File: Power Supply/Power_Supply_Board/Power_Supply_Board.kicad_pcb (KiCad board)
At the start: 2 copper layers, 36 parts

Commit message: Power Supply Board Progress
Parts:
- C1, C3: footprint Capacitor_THT:CP_Axial_L30.0mm_D18.0mm_P35.00mm_Horizontal -> Capacitor_THT:CP_Axial_L55.0mm_D26.0mm_P60.00mm_Horizontal
- C2, C4: footprint Capacitor_THT:CP_Axial_L30.0mm_D18.0mm_P35.00mm_Horizontal -> Capacitor_THT:CP_Axial_L55.0mm_D26.0mm_P60.00mm_Horizontal; moved to B.Cu
- C5, C6, C7: footprint Capacitor_THT:CP_Axial_L38.0mm_D21.0mm_P44.00mm_Horizontal -> Capacitor_THT:CP_Axial_L42.0mm_D26.0mm_P45.00mm_Horizontal
- moved C3 59.4 mm to (150.3, 115.3), turned to 180 degrees
- moved TP12 56.9 mm to (180.8, 85.7)
- moved R1 49.0 mm to (97.4, 101.0)
- moved C4 47.7 mm to (150.3, 119.0), turned to 180 degrees
- moved R2 44.7 mm to (122.8, 101.0)
- moved D2 42.1 mm to (81.4, 121.8)
- moved D1 41.6 mm to (81.4, 135.5)
- moved D6 41.3 mm to (89.1, 145.7), turned to 90 degrees
- moved D4 39.9 mm to (85.3, 121.8)
- moved D5 39.5 mm to (92.9, 145.7), turned to 90 degrees
- moved D3 39.3 mm to (85.3, 135.5)
- moved TP1 36.1 mm to (83.3, 97.7)
- moved TP10 34.6 mm to (81.3, 149.9)
- moved TP11 31.5 mm to (85.5, 149.9)
- moved C7 30.5 mm to (222.4, 137.6)
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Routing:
- net Net-(C1-Pad2): track 0.00 -> 81.2 mm
- net Net-(D2-K): track 0.00 -> 70.8 mm
- net F: track 0.00 -> 31.5 mm
- net G: track 0.00 -> 28.8 mm
- net B: track 0.00 -> 28.1 mm
- net C: track 0.00 -> 27.9 mm
- net Net-(C8-Pad2): track 0.00 -> 24.2 mm
- net D: track 0.00 -> 20.3 mm
- net Net-(D6-A): track 0.00 -> 8.88 mm
- net 60VAC: track 0.00 -> 8.14 mm
- net Net-(D5-A): track 0.00 -> 4.97 mm
- net Net-(D3-A): track 0.00 -> 4.39 mm
- net Net-(D1-A): track 0.00 -> 4.37 mm
- net Net-(D1-K): track 0.00 -> 3.53 mm
- net Net-(D3-K): track 0.00 -> 3.53 mm
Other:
- board text added: "HCF Power Supply"
- board text added: "Might not need the reservoir cap labels. just keep a little buffer on the edge, but otherwise, order doesnt matter just polarity"
- board text added: "Ver 1.0"

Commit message: Power Supply Board Progress
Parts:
- moved C1 3.95 mm to (90.3, 86.7)
- moved C2 3.95 mm to (90.3, 82.7)
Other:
- board text removed: "Might not need the reservoir cap labels. just keep a little buffer on the edge, but otherwise, order doesnt matter just polarity"
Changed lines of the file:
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@@
 	(footprint "Capacitor_THT:CP_Axial_L55.0mm_D26.0mm_P60.00mm_Horizontal"
 		(layer "F.Cu")
-		(at 90.302 82.7075)
+		(at 90.3 86.6525)
 		(descr "CP, Axial series, Axial, Horizontal, pin pitch=60mm, , length*diameter=55*26mm^2, Electrolytic Capacitor, , http://www.vishay.com/docs/42037/53d.pdf")
 		(tags "CP Axial series Axial Horizontal pin pitch 60mm  length 55mm diameter 26mm Electrolytic Capacitor")
@@
 	(footprint "Capacitor_THT:CP_Axial_L55.0mm_D26.0mm_P60.00mm_Horizontal"
 		(layer "B.Cu")
-		(at 90.3 86.6525)
+		(at 90.302 82.7075)
 		(descr "CP, Axial series, Axial, Horizontal, pin pitch=60mm, , length*diameter=55*26mm^2, Electrolytic Capacitor, , http://www.vishay.com/docs/42037/53d.pdf")
 		(tags "CP Axial series Axial Horizontal pin pitch 60mm  length 55mm diameter 26mm Electrolytic Capacitor")
@@
 		)
 		(property "Value" "220uF 300V"
-			(at 30.43 -2.4 180)
+			(at 30.348 1.7475 180)
 			(layer "B.SilkS")
 			(effects
@@
 			)
 			(justify left bottom)
-		)
-	)
-	(gr_text "Might not need the reservoir cap labels. just keep a little buffer on the edge, but otherwise, order doesnt matter just polarity"
-		(at 94.2 72.26 0)
-		(layer "Edge.Cuts")
-		(effects
-			(font
-				(size 1 1)
-				(thickness 0.15)
-			)
-			(justify left bottom)

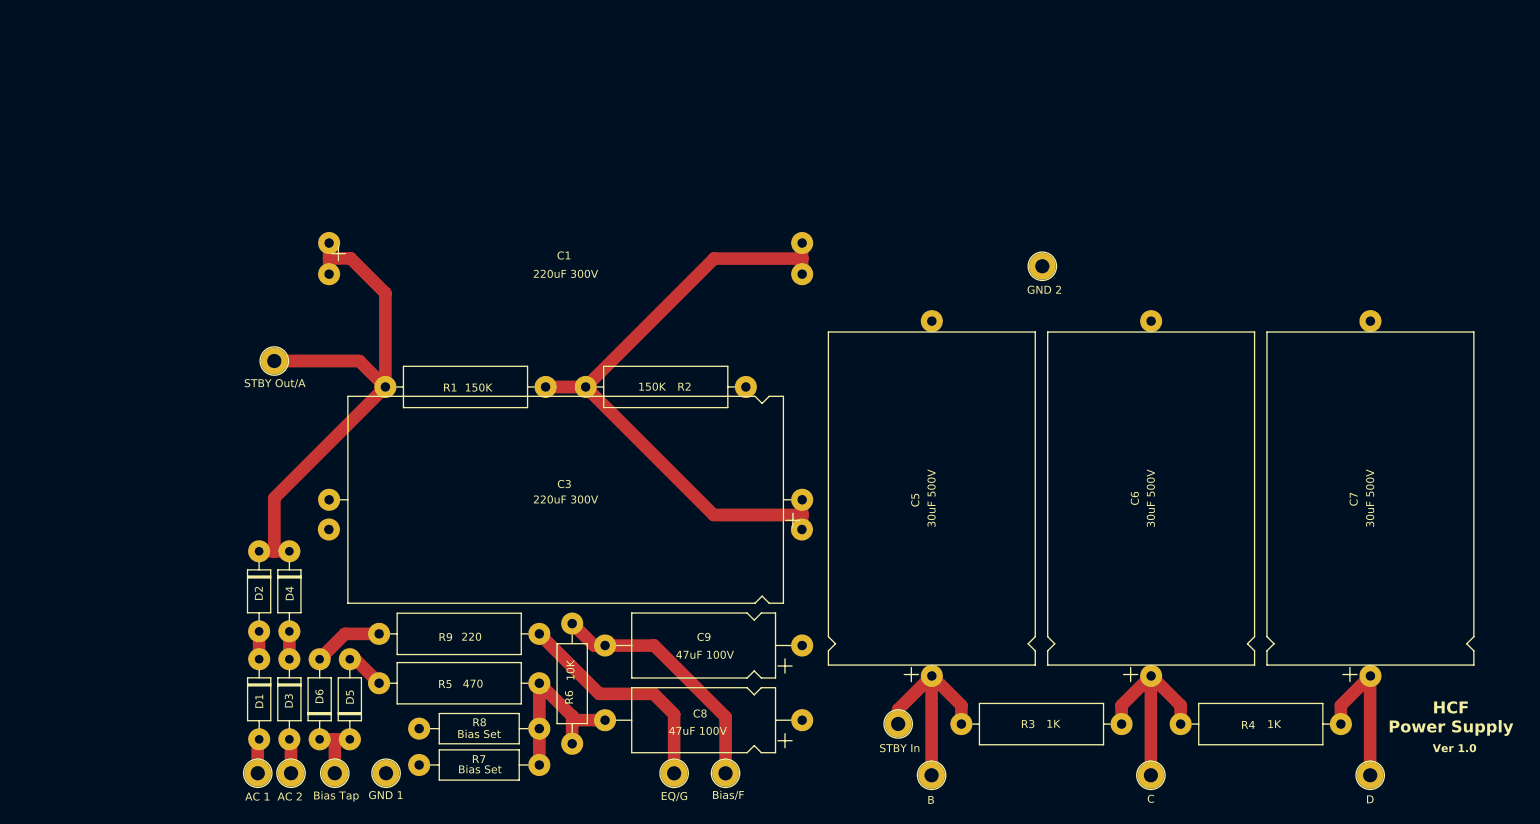
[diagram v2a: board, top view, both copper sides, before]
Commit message: Completed Initial Mockup of Power Supply Board PCB
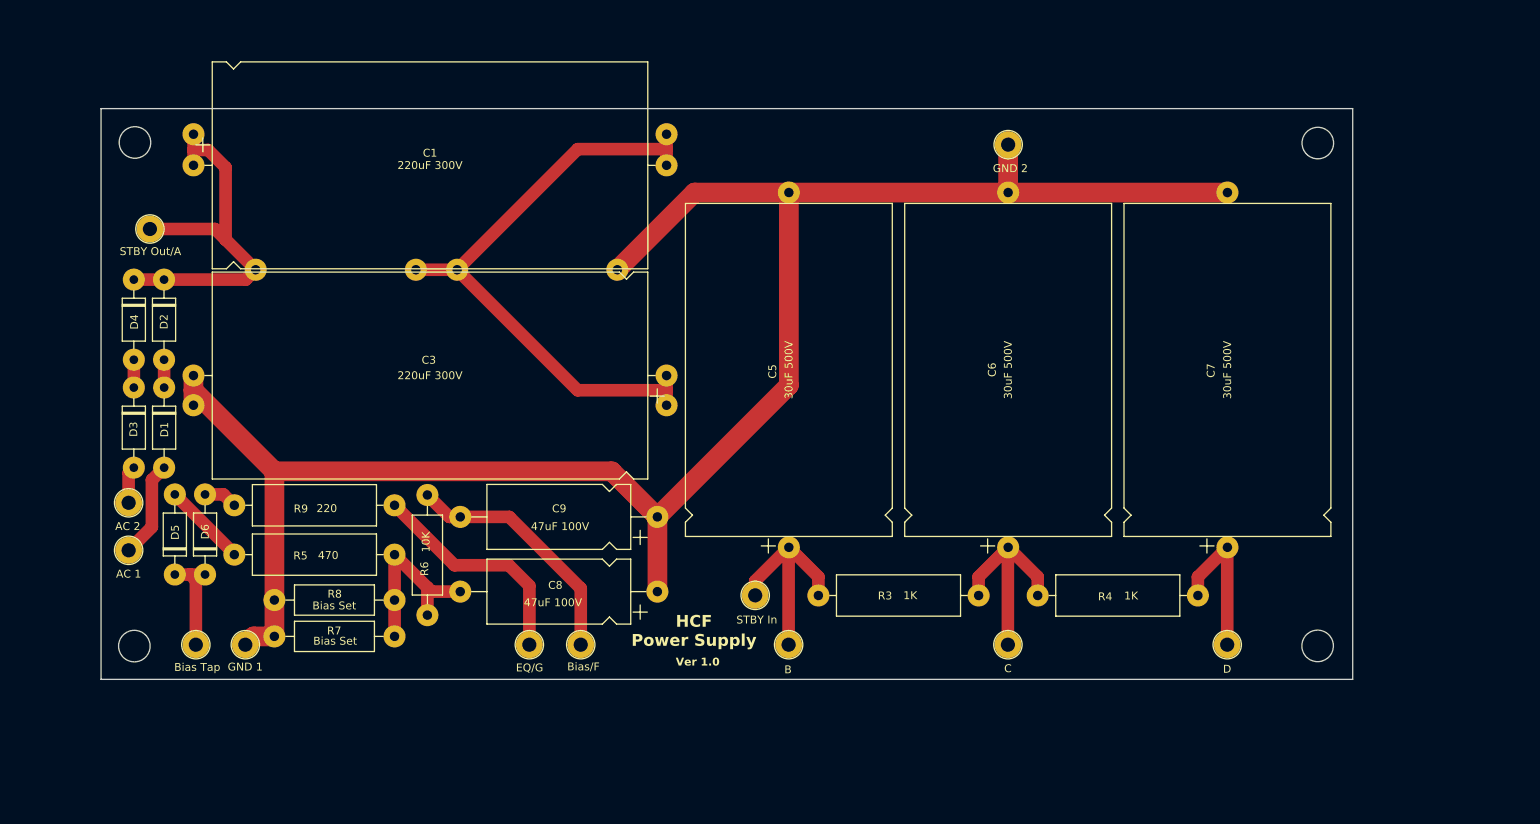
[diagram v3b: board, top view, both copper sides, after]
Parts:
- added REF**: MountingHole_4mm, MountingHole:MountingHole_4mm, F.Cu at (215.7, 70.0)
- added REF**: MountingHole_4mm, MountingHole:MountingHole_4mm, F.Cu at (215.7, 133.8)
- added REF**: MountingHole_4mm, MountingHole:MountingHole_4mm, F.Cu at (65.7, 70.0)
- added REF**: MountingHole_4mm, MountingHole:MountingHole_4mm, F.Cu at (65.6, 133.8)
- R1, R2: moved to B.Cu
- moved TP11 40.0 mm to (64.9, 115.7)
- moved D3 39.7 mm to (65.5, 101.0)
- moved D4 39.7 mm to (65.5, 87.3)
- moved D1 36.5 mm to (69.4, 101.0)
- moved D2 36.5 mm to (69.4, 87.3)
- moved TP10 32.7 mm to (64.9, 121.7)
- moved D5 30.5 mm to (70.7, 124.8)
- moved D6 25.5 mm to (74.6, 124.8)
- moved R6 24.6 mm to (102.8, 114.7)
- moved TP8 24.6 mm to (115.7, 133.7)
- moved R5 24.6 mm to (78.3, 122.2)
- moved R7 24.6 mm to (98.6, 132.6)
- moved R9 24.6 mm to (78.3, 116.0)
- moved TP7 24.6 mm to (122.2, 133.7)
- moved C9 24.6 mm to (131.9, 117.4)
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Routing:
- net GND: track 0.00 -> 239.3 mm
- net Net-(D2-K): track 70.8 -> 49.6 mm
- net Net-(D1-A): track 4.37 -> 12.3 mm
- net Net-(D5-A): track 4.97 -> 10.8 mm
- net 60VAC: track 8.14 -> 13.0 mm
- net Net-(D6-A): track 8.88 -> 4.28 mm
- net Net-(C1-Pad2): track 81.2 -> 78.7 mm
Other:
- board outline added: 158.8 x 72.4 mm
